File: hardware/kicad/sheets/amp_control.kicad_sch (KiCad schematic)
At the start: 10 parts, among them J8 AMP REM / GND, J9 AMP SIGNAL IN / GND, Q5 BSS138, Q6 BSS84

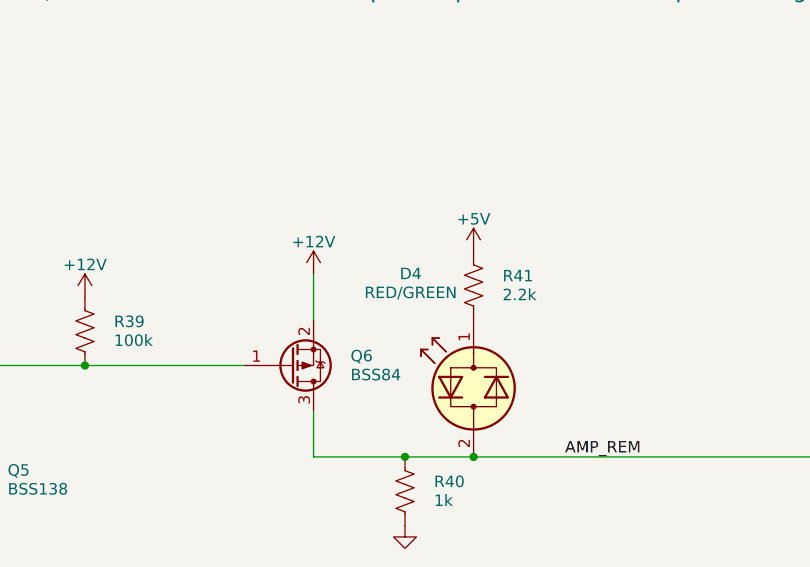
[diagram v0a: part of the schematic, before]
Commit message: Put supply pins on top and grounds on the bottom of IC symbols; flake8-clean Python
Schematic: re-laid out pins on U2, U3, U6, U7, U11, U14, U17-U20, U22-U24
and PS1 (supply on top, ground/strap pins on the bottom edge) via custom
`cryocooler:` symbols (make_lib.from_stock) and a gnd_bus helper; U18/U2
use mirroring instead of a 180 degree rotation. Nets are unchanged (ERC 0,
117/117 datasheet rules, PCB nets still match). Text placement now shows
every power-symbol name, avoids wires, and uses a realistic character width.

Python: black -l 79 -S plus manual wrapping so hardware/kicad and scripts/
pass flake8; add .flake8.

Co-Authored-By: Claude Sonnet 5.5 <noreply@anthropic.com>
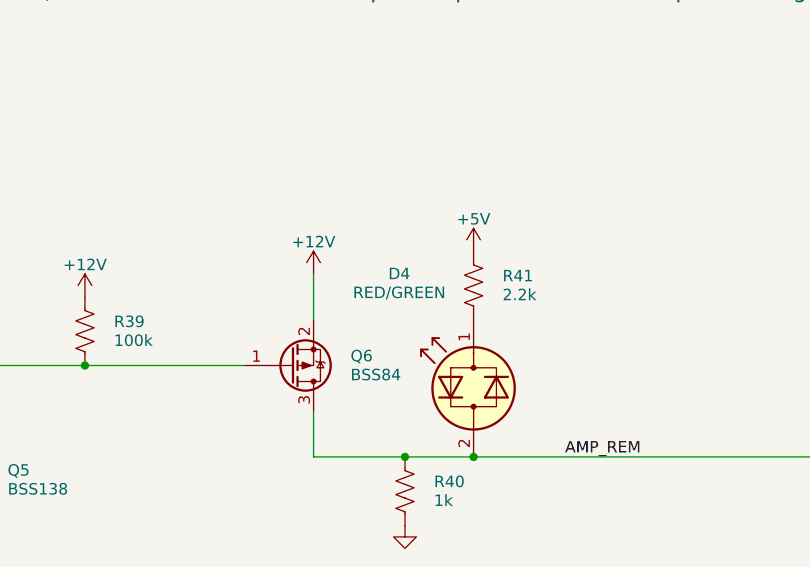
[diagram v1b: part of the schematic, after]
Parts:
- removed D4: RED/GREEN, LED_SMD:LED_1206_3216Metric, symbol Device:LED_Dual_Bidirectional
- removed J9: AMP SIGNAL IN / GND, TerminalBlock_Phoenix:TerminalBlock_Phoenix_MKDS-1,5-2-5.08_1x02_P5.08mm_Horizontal, symbol Connector:Screw_Terminal_01x02
- added J8: AMP REM / GND, TerminalBlock_Phoenix:TerminalBlock_Phoenix_MKDS-1,5-2-5.08_1x02_P5.08mm_Horizontal, symbol Connector:Screw_Terminal_01x02
- added R38: 100k, Resistor_SMD:R_0603_1608Metric, symbol Device:R_US
- D4: renamed from R41; value 2.2k -> RED/GREEN; footprint Resistor_SMD:R_0603_1608Metric -> LED_SMD:LED_1206_3216Metric; symbol Device:R_US -> Device:LED_Dual_Bidirectional
- J9: renamed from J8; value AMP REM / GND -> AMP SIGNAL IN / GND
- Q5: renamed from R38; value 100k -> BSS138; footprint Resistor_SMD:R_0603_1608Metric -> Package_TO_SOT_SMD:SOT-23; symbol Device:R_US -> Transistor_FET:BSS138
- Q6: renamed from R39; value 100k -> BSS84; footprint Resistor_SMD:R_0603_1608Metric -> Package_TO_SOT_SMD:SOT-23; symbol Device:R_US -> Transistor_FET:BSS84
- R39: renamed from Q5; value BSS138 -> 100k; footprint Package_TO_SOT_SMD:SOT-23 -> Resistor_SMD:R_0603_1608Metric; symbol Transistor_FET:BSS138 -> Device:R_US
- R40: renamed from Q6; value BSS84 -> 1k; footprint Package_TO_SOT_SMD:SOT-23 -> Resistor_SMD:R_0603_1608Metric; symbol Transistor_FET:BSS84 -> Device:R_US
- R41: renamed from R40; value 1k -> 2.2k
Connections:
- net +12V: now also Q6.2 (S), R39.1; no longer Q6.1, R40.2 (S)
- net +5V: now also R41.1; no longer D4.1
- net AMP_REM: now also D4.2 (AK), Q6.3 (D), R40.1, J8.1 (Pin_1); no longer J9.1 (Pin_1), R40.3 (D), R41.1
- net GND: now also R40.2, J8.2 (Pin_2), R38.2; no longer R39.2 (S), R41.2
- net SIG_SINE: now also J9.1 (Pin_1)
- net at Q5.1 (G), R37.2: now also R38.1; no longer R39.1 (G)
- new net: D4.1 (KA), R41.2
- new net: Q5.3 (D), Q6.1 (G), R39.2
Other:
- moved on the sheet: J9, R41

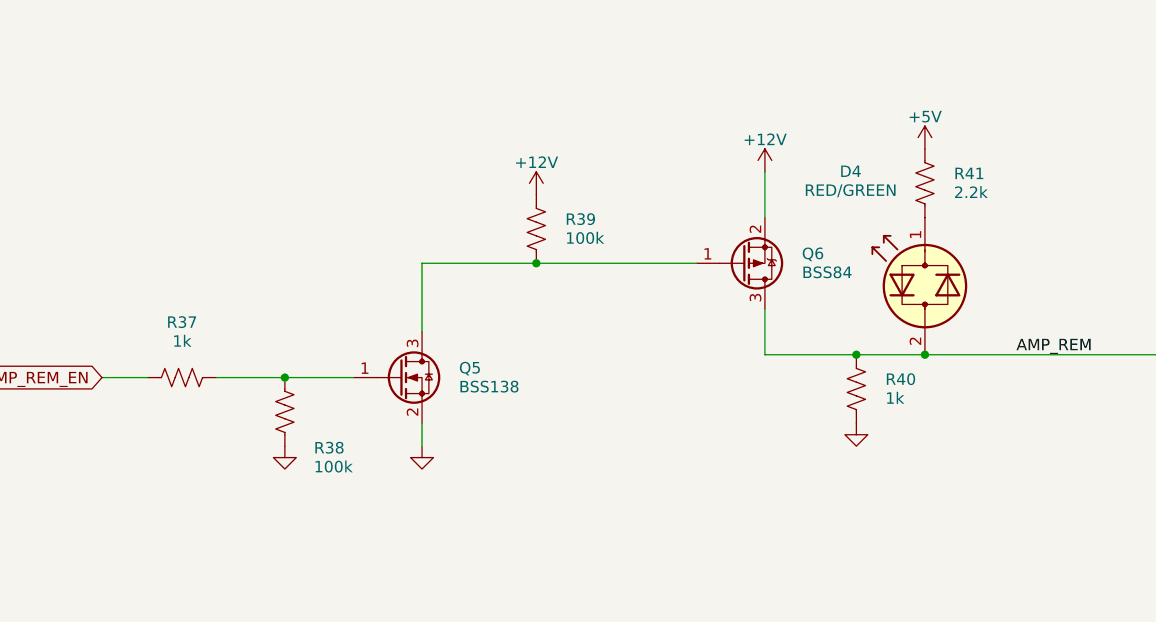
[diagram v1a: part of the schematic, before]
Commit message: KiCad schematic: INA239, ADS1220, SC18IS604 bridge, relay driver, test points
- system_current: INA237 -> INA239 (SPI, CS GPIO3) with the 49.9 ohm / 470 nF
  input filter, power LED and ALERT LED; VBUS shares the filtered IN- node.
- cold_head: ADS122C04 -> ADS1220 (SPI, CS GPIO44).
- i2c_bridge (new): SC18IS604 SPI-to-I2C bridge for the EMC2303, with a
  74LVC1G125 gating its MISO onto the shared bus.
- compressor_relay (new): GPIO16 high-side switch sharing one generator
  function with the amplifier REM switch.
- debug (new): about 40 test points and rail LEDs (the isolated rail LED
  returns to ISO_GND).
- ISO7741 -> ACS37800 SPI lines are straight wires (pins reordered on the
  symbol); USB_VBUS is one wire plus a naming label.
- Custom symbols for INA239, ADS1220, SC18IS604; datasheet rules 117 -> 162;
  GPIO map checks updated. ERC 0.

Co-Authored-By: Claude Sonnet 5.5 <noreply@anthropic.com>
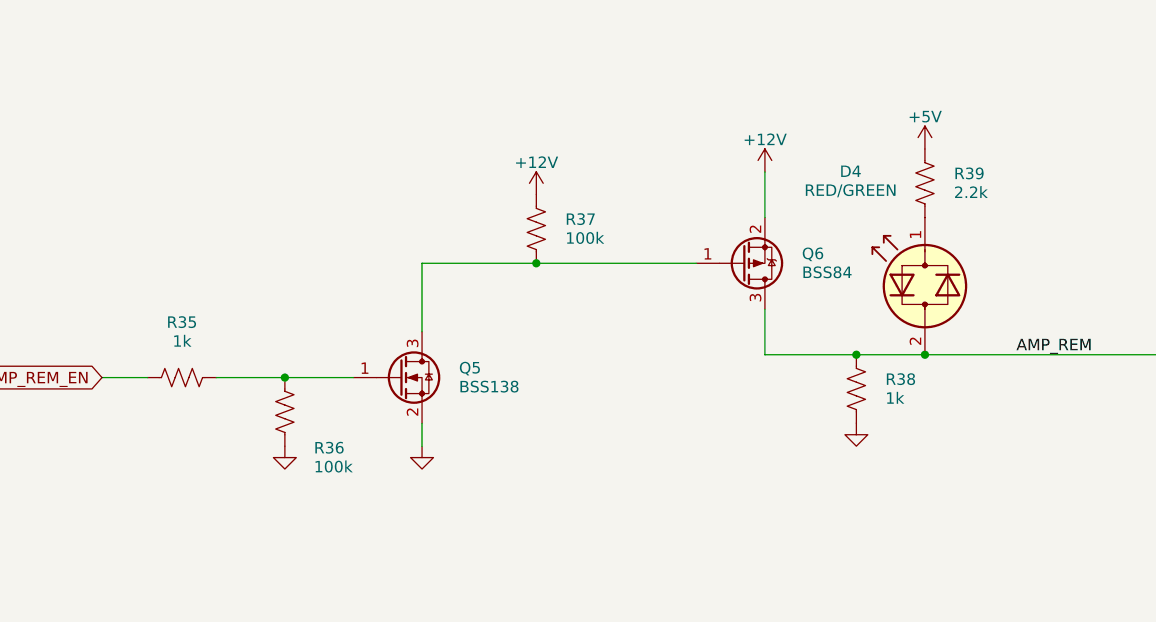
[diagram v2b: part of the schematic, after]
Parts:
- removed J8: AMP REM / GND, TerminalBlock_Phoenix:TerminalBlock_Phoenix_MKDS-1,5-2-5.08_1x02_P5.08mm_Horizontal, symbol Connector:Screw_Terminal_01x02
- removed J9: AMP SIGNAL IN / GND, TerminalBlock_Phoenix:TerminalBlock_Phoenix_MKDS-1,5-2-5.08_1x02_P5.08mm_Horizontal, symbol Connector:Screw_Terminal_01x02
- removed Q5: BSS138, Package_TO_SOT_SMD:SOT-23, symbol Transistor_FET:BSS138
- removed R40: 1k, Resistor_SMD:R_0603_1608Metric, symbol Device:R_US
- added D4: RED/GREEN, LED_SMD:LED_1206_3216Metric, symbol Device:LED_Dual_Bidirectional
- added R35: 1k, Resistor_SMD:R_0603_1608Metric, symbol Device:R_US
- added R36, R37: 100k, Resistor_SMD:R_0603_1608Metric, symbol Device:R_US
- J8: renamed from R41; value 2.2k -> AMP REM / GND; footprint Resistor_SMD:R_0603_1608Metric -> TerminalBlock_Phoenix:TerminalBlock_Phoenix_MKDS-1,5-2-5.08_1x02_P5.08mm_Horizontal; symbol Device:R_US -> Connector:Screw_Terminal_01x02
- J9: renamed from D4; value RED/GREEN -> AMP SIGNAL IN / GND; footprint LED_SMD:LED_1206_3216Metric -> TerminalBlock_Phoenix:TerminalBlock_Phoenix_MKDS-1,5-2-5.08_1x02_P5.08mm_Horizontal; symbol Device:LED_Dual_Bidirectional -> Connector:Screw_Terminal_01x02
- Q5: renamed from R37; value 1k -> BSS138; footprint Resistor_SMD:R_0603_1608Metric -> Package_TO_SOT_SMD:SOT-23; symbol Device:R_US -> Transistor_FET:BSS138
- R38: value 100k -> 1k
- R39: value 100k -> 2.2k
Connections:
- net +12V: now also R37.1; no longer R39.1
- net +5V: now also R39.1; no longer J8.1
- net AMP_REM: now also J8.1 (Pin_1), R38.1, D4.2 (AK); no longer J9.2 (AK)
- net AMP_REM_EN: now also R35.1; no longer Q5.1
- net GND: now also J8.2 (Pin_2), J9.2 (Pin_2), Q5.2 (S), R36.2
- net SIG_SINE: now also J9.1 (Pin_1)
- net at Q6.1 (G): now also Q5.3 (D), R37.2; no longer R39.2
- new net: Q5.1 (G), R35.2, R36.1
- new net: D4.1 (KA), R39.2
